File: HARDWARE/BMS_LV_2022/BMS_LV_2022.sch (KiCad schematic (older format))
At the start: 30 parts, among them J1 Conn_01x06_Male, J2 Conn_01x12_Male, J3 USB_B_Mini, J4 Battery+, J5 Battery-, SW1 SW_Push, U1 STM32L4P5RET6, Y1 Crystal

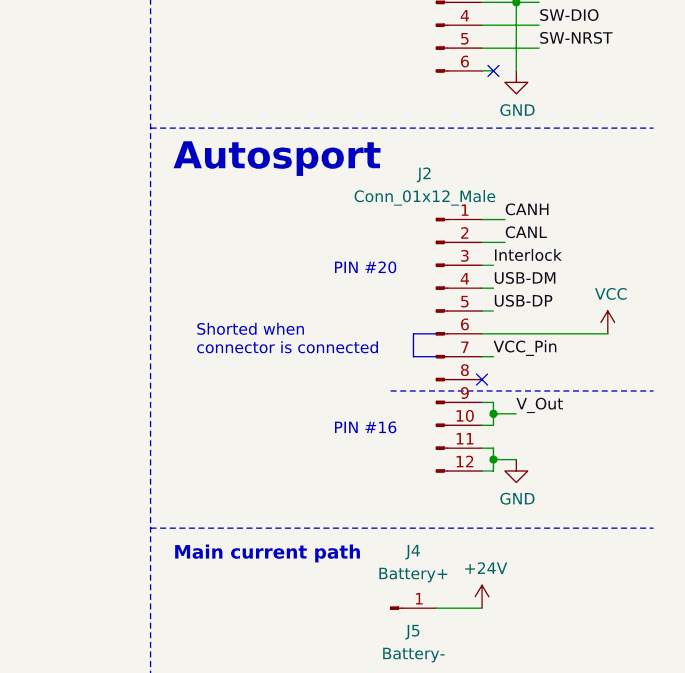
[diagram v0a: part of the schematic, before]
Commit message: PCB Routing Update
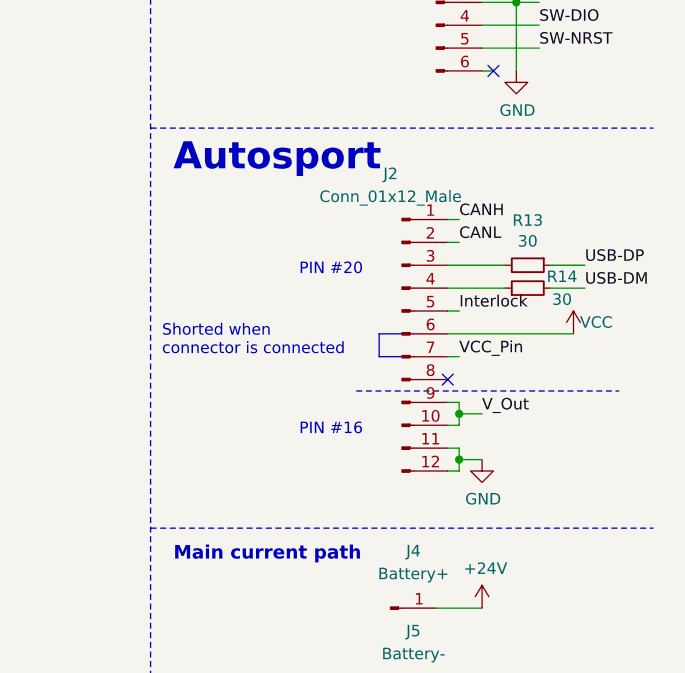
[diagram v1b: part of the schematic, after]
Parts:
- added R13, R14: 30, Resistor_SMD:R_0603_1608Metric, symbol Device:R_Small
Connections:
- net Interlock: now also J2.5 (Pin_5); no longer J2.3 (Pin_3)
- net USB-DM: now also R14.2; no longer J2.4 (Pin_4)
- net USB-DP: now also R13.1; no longer J2.5 (Pin_5)
- new net: J2.3 (Pin_3), R13.2
- new net: J2.4 (Pin_4), R14.1
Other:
- moved on the sheet: J2
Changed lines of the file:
@@
 EESchema Schematic File Version 4
-LIBS:BMS_LV_2022-cache
-EELAYER 29 0
+EELAYER 30 0
 EELAYER END
 $Descr A4 11693 8268
@@
 L Connector:Conn_01x12_Male J2
 U 1 1 61E8A62C
-P 10250 4150
-F 0 "J2" H 10200 4850 50  0000 C CNN
-F 1 "Conn_01x12_Male" H 10200 4750 50  0000 C CNN
-F 2 "footprints:AS214-97PN" H 10250 4150 50  0001 C CNN
-F 3 "~" H 10250 4150 50  0001 C CNN
-	1    10250 4150
+P 10100 4150
+F 0 "J2" H 10050 4850 50  0000 C CNN
+F 1 "Conn_01x12_Male" H 10050 4750 50  0000 C CNN
+F 2 "footprints:AS214-97PN" H 10100 4150 50  0001 C CNN
+F 3 "~" H 10100 4150 50  0001 C CNN
+	1    10100 4150
 	1    0    0    -1
 $EndComp
@@
 Text Label 800  4650 2    50   ~ 0
 CANL
-Text Label 10550 3650 0    50   ~ 0
+Text Label 10350 3650 0    50   ~ 0
 CANH
-Text Label 10550 3750 0    50   ~ 0
+Text Label 10350 3750 0    50   ~ 0
 CANL
-Wire Wire Line
-	10550 3650 10450 3650
-Wire Wire Line
-	10450 3750 10550 3750
 $Sheet
 S 550  2950 1050 500
@@
 Text Label 7000 4300 0    50   ~ 0
 Interlock
-Text Label 10500 3850 0    50   ~ 0
+Text Label 10350 4050 0    50   ~ 0
 Interlock
 Wire Wire Line
-	10450 3850 10500 3850
+	10300 4050 10350 4050
 Wire Wire Line
 	1600 3350 1650 3350
 Text Label 1650 3350 0    50   ~ 0
 CS_IP+
-Text Label 10600 4500 0    50   ~ 0
+Text Label 10450 4500 0    50   ~ 0
 V_Out
 Wire Wire Line
-	10450 4750 10500 4750
+	10300 4750 10350 4750
 $Comp
 L power:GND #PWR010
 U 1 1 62A04D91
-P 10600 4700
-F 0 "#PWR010" H 10600 4450 50  0001 C CNN
-F 1 "GND" H 10605 4527 50  0000 C CNN
-F 2 "" H 10600 4700 50  0001 C CNN
-F 3 "" H 10600 4700 50  0001 C CNN
-	1    10600 4700
-	1    0    0    -1
-$EndComp
-Wire Wire Line
-	10500 4550 10450 4550
-Text Notes 9200 4250 0    50   ~ 0
+P 10450 4700
+F 0 "#PWR010" H 10450 4450 50  0001 C CNN
+F 1 "GND" H 10455 4527 50  0000 C CNN
+F 2 "" H 10450 4700 50  0001 C CNN
+F 3 "" H 10450 4700 50  0001 C CNN
+	1    10450 4700
+	1    0    0    -1
+$EndComp
+Wire Wire Line
+	10350 4550 10300 4550
+Text Notes 9050 4250 0    50   ~ 0
 Shorted when \nconnector is connected
 Text Notes 9450 700  0    157  ~ 31
@@
 VCC_Pin
 Wire Wire Line
-	10450 4250 10500 4250
-Text Label 10500 4250 0    50   ~ 0
+	10300 4250 10350 4250
+Text Label 10350 4250 0    50   ~ 0
 VCC_Pin
 Wire Bus Line
-	10250 4250 10150 4250
+	10100 4250 10000 4250
 Wire Bus Line
-	10150 4250 10150 4150
+	10000 4250 10000 4150
 Wire Bus Line
-	10150 4150 10250 4150
+	10000 4150 10100 4150
 Wire Notes Line
-	10050 4400 11200 4400
-Text Notes 9800 3900 0    50   ~ 0
+	9900 4400 11050 4400
+Text Notes 9650 3900 0    50   ~ 0
 PIN #20
-Text Notes 9800 4600 0    50   ~ 0
+Text Notes 9650 4600 0    50   ~ 0
 PIN #16
-Text Label 10500 3950 0    50   ~ 0
-USB-DM
-Text Label 10500 4050 0    50   ~ 0
-USB-DP
-Wire Wire Line
-	10450 3950 10500 3950
-Wire Wire Line
-	10450 4050 10500 4050
 NoConn ~ 5550 5300
 NoConn ~ 5550 5400
@@
 NoConn ~ 6950 5500
 NoConn ~ 6950 5600
-NoConn ~ 10450 4350
+NoConn ~ 10300 4350
 NoConn ~ 10350 1500
 Text Notes 1200 5200 0    118  ~ 0
@@
 	6150 1800 6150 1700
 Wire Wire Line
-	10450 4150 11000 4150
+	10300 4150 10850 4150
 $Comp
 L power:VCC #PWR014
 U 1 1 622C0542
-P 11000 4150
-F 0 "#PWR014" H 11000 4000 50  0001 C CNN
-F 1 "VCC" H 11015 4323 50  0000 C CNN
-F 2 "" H 11000 4150 50  0001 C CNN
-F 3 "" H 11000 4150 50  0001 C CNN
-	1    11000 4150
-	1    0    0    -1
-$EndComp
-Wire Wire Line
-	10500 4450 10450 4450
-Wire Wire Line
-	10500 4450 10500 4500
-Wire Wire Line
-	10500 4500 10600 4500
-Connection ~ 10500 4500
-Wire Wire Line
-	10500 4500 10500 4550
-Wire Wire Line
-	10500 4750 10500 4700
-Wire Wire Line
-	10500 4650 10450 4650
-Wire Wire Line
-	10500 4700 10600 4700
-Connection ~ 10500 4700
-Wire Wire Line
-	10500 4700 10500 4650
+P 10850 4150
+F 0 "#PWR014" H 10850 4000 50  0001 C CNN
+F 1 "VCC" H 10950 4200 50  0000 C CNN
+F 2 "" H 10850 4150 50  0001 C CNN
+F 3 "" H 10850 4150 50  0001 C CNN
+	1    10850 4150
+	1    0    0    -1
+$EndComp
+Wire Wire Line
+	10350 4450 10300 4450
+Wire Wire Line
+	10350 4450 10350 4500
+Wire Wire Line
+	10350 4500 10450 4500
+Connection ~ 10350 4500
+Wire Wire Line
+	10350 4500 10350 4550
+Wire Wire Line
+	10350 4750 10350 4700
+Wire Wire Line
+	10350 4650 10300 4650
+Wire Wire Line
+	10350 4700 10450 4700
+Connection ~ 10350 4700
+Wire Wire Line
+	10350 4700 10350 4650
 $Comp
 L Device:Crystal_GND24_Small Y1
@@
 	1    0    0    -1
 $EndComp
+$Comp
+L Device:R_Small R14
+U 1 1 61EF25B8
+P 10650 3950
+F 0 "R14" V 10700 3800 50  0000 C CNN
+F 1 "30" V 10600 3800 50  0000 C CNN
+F 2 "Resistor_SMD:R_0603_1608Metric" H 10650 3950 50  0001 C CNN
+F 3 "~" H 10650 3950 50  0001 C CNN
+	1    10650 3950
+	0    -1   -1   0
+$EndComp
+Wire Wire Line
+	10900 3950 10750 3950
+Wire Wire Line
+	10900 3850 10750 3850
+Text Label 10900 3950 0    50   ~ 0
+USB-DM
+Text Label 10900 3850 0    50   ~ 0
+USB-DP
+$Comp
+L Device:R_Small R13
+U 1 1 61EF25C3
+P 10650 3850
+F 0 "R13" V 10454 3850 50  0000 C CNN
+F 1 "30" V 10545 3850 50  0000 C CNN
+F 2 "Resistor_SMD:R_0603_1608Metric" H 10650 3850 50  0001 C CNN
+F 3 "~" H 10650 3850 50  0001 C CNN
+	1    10650 3850
+	0    1    1    0
+$EndComp
+Wire Wire Line
+	10300 3650 10350 3650
+Wire Wire Line
+	10300 3750 10350 3750
+Wire Wire Line
+	10550 3950 10300 3950
+Wire Wire Line
+	10550 3850 10300 3850
 $EndSCHEMATC

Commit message: PCB Routing Update 2
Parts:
- U1: symbol BMS_LV_2022-rescue:STM32L4P5RET6-STM32L4P5RET6 -> stm32l4p5ret6:STM32L4P5RET6-STM32L4P5RET6
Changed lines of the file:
@@
 CS
 $Comp
-L BMS_LV_2022-rescue:STM32L4P5RET6-STM32L4P5RET6 U1
+L stm32l4p5ret6:STM32L4P5RET6-STM32L4P5RET6 U1
 U 1 1 61992FF1
 P 6250 3900

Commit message: Small bug fixes
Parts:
- U1: symbol stm32l4p5ret6:STM32L4P5RET6-STM32L4P5RET6 -> BMS_LV_2022-rescue:STM32L4P5RET6-STM32L4P5RET6-stm32l4p5ret6
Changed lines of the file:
@@
 CS
 $Comp
-L stm32l4p5ret6:STM32L4P5RET6-STM32L4P5RET6 U1
+L BMS_LV_2022-rescue:STM32L4P5RET6-STM32L4P5RET6-stm32l4p5ret6 U1
 U 1 1 61992FF1
 P 6250 3900

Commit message: HARDWARE Release V1.0
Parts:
- added R15: 1k, Resistor_SMD:R_0603_1608Metric, symbol Device:R_Small
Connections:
- net Interlock: now also R15.2; no longer J2.5 (Pin_5)
- net Therm_1: now also U1.17 (PA3); no longer U1.20 (PA4)
- net Therm_2: now also U1.20 (PA4); no longer U1.21 (PA5)
- net Therm_3: now also U1.21 (PA5); no longer U1.22 (PA6)
- net Therm_4: now also U1.22 (PA6); no longer U1.23 (PA7)
- net Therm_5: now also U1.23 (PA7); no longer U1.24 (PC4)
- net Therm_6: now also U1.24 (PC4); no longer U1.25 (PC5)
- net Therm_8: now reaches U1.26 (PB0)
- new net: J2.5 (Pin_5), R15.1
- new net Therm_7: U1.25 (PC5)
- no-connect marks 29 -> 27
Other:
- moved on the sheet: C1, D1, D3, D4, D5, R1, R2, R3, R5, R6, SW1

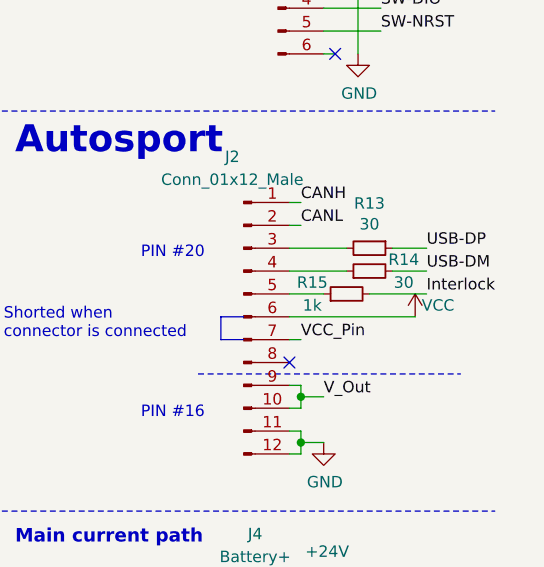
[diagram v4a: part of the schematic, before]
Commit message: Changes in V1.0
-Fuse holder change
-Autosport conn angle change
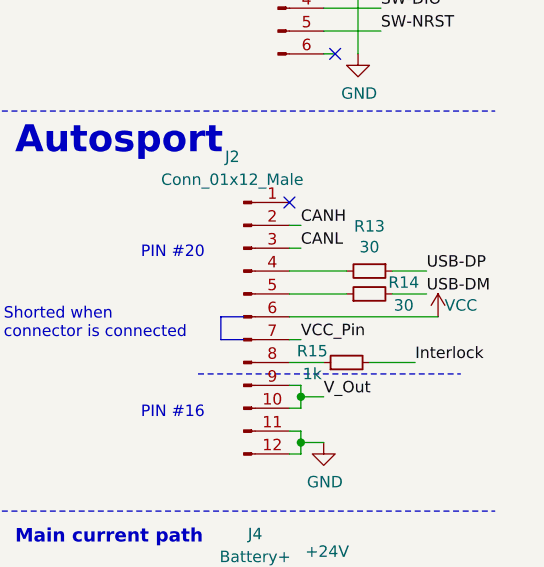
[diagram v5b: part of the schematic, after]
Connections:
- net CANH: now also J2.2 (Pin_2); no longer J2.1 (Pin_1)
- net CANL: now also J2.3 (Pin_3); no longer J2.2 (Pin_2)
- net at R13.2: now also J2.4 (Pin_4); no longer J2.3 (Pin_3)
- net at R14.1: now also J2.5 (Pin_5); no longer J2.4 (Pin_4)
- net at R15.1: now also J2.8 (Pin_8); no longer J2.5 (Pin_5)
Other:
- moved on the sheet: R13, R14, R15
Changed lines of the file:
@@
 Text Label 800  4800 2    50   ~ 0
 CANL
-Text Label 10350 3650 0    50   ~ 0
+Text Label 10350 3750 0    50   ~ 0
 CANH
-Text Label 10350 3750 0    50   ~ 0
+Text Label 10350 3850 0    50   ~ 0
 CANL
 $Sheet
@@
 Text Label 7000 4300 0    50   ~ 0
 Interlock
-Text Label 10900 4050 0    50   ~ 0
+Text Label 10850 4350 0    50   ~ 0
 Interlock
 Wire Wire Line
@@
 NoConn ~ 6950 5500
 NoConn ~ 6950 5600
-NoConn ~ 10300 4350
+NoConn ~ 10300 3650
 NoConn ~ 10350 1500
 Text Notes 1200 5350 0    118  ~ 0
@@
 Wire Wire Line
 	6150 1800 6150 1700
-Wire Wire Line
-	10300 4150 10850 4150
 $Comp
 L power:VCC #PWR014
 U 1 1 622C0542
-P 10850 4150
-F 0 "#PWR014" H 10850 4000 50  0001 C CNN
-F 1 "VCC" H 10950 4200 50  0000 C CNN
-F 2 "" H 10850 4150 50  0001 C CNN
-F 3 "" H 10850 4150 50  0001 C CNN
-	1    10850 4150
+P 10950 4150
+F 0 "#PWR014" H 10950 4000 50  0001 C CNN
+F 1 "VCC" H 11050 4200 50  0000 C CNN
+F 2 "" H 10950 4150 50  0001 C CNN
+F 3 "" H 10950 4150 50  0001 C CNN
+	1    10950 4150
 	1    0    0    -1
 $EndComp
@@
 L Device:R_Small R14
 U 1 1 61EF25B8
+P 10650 4050
+F 0 "R14" V 10700 3900 50  0000 C CNN
+F 1 "30" V 10600 3900 50  0000 C CNN
+F 2 "Resistor_SMD:R_0603_1608Metric" H 10650 4050 50  0001 C CNN
+F 3 "~" H 10650 4050 50  0001 C CNN
+	1    10650 4050
+	0    -1   -1   0
+$EndComp
+Wire Wire Line
+	10900 4050 10750 4050
+Wire Wire Line
+	10900 3950 10750 3950
+Text Label 10900 4050 0    50   ~ 0
+USB-DM
+Text Label 10900 3950 0    50   ~ 0
+USB-DP
+$Comp
+L Device:R_Small R13
+U 1 1 61EF25C3
 P 10650 3950
-F 0 "R14" V 10700 3800 50  0000 C CNN
-F 1 "30" V 10600 3800 50  0000 C CNN
+F 0 "R13" V 10454 3950 50  0000 C CNN
+F 1 "30" V 10545 3950 50  0000 C CNN
 F 2 "Resistor_SMD:R_0603_1608Metric" H 10650 3950 50  0001 C CNN
 F 3 "~" H 10650 3950 50  0001 C CNN
 	1    10650 3950
-	0    -1   -1   0
-$EndComp
-Wire Wire Line
-	10900 3950 10750 3950
-Wire Wire Line
-	10900 3850 10750 3850
-Text Label 10900 3950 0    50   ~ 0
-USB-DM
-Text Label 10900 3850 0    50   ~ 0
-USB-DP
-$Comp
-L Device:R_Small R13
-U 1 1 61EF25C3
-P 10650 3850
-F 0 "R13" V 10454 3850 50  0000 C CNN
-F 1 "30" V 10545 3850 50  0000 C CNN
-F 2 "Resistor_SMD:R_0603_1608Metric" H 10650 3850 50  0001 C CNN
-F 3 "~" H 10650 3850 50  0001 C CNN
-	1    10650 3850
 	0    1    1    0
 $EndComp
 Wire Wire Line
-	10300 3650 10350 3650
-Wire Wire Line
 	10300 3750 10350 3750
 Wire Wire Line
+	10300 3850 10350 3850
+Wire Wire Line
+	10550 4050 10300 4050
+Wire Wire Line
 	10550 3950 10300 3950
-Wire Wire Line
-	10550 3850 10300 3850
 $Comp
 L Device:R_Small R15
 U 1 1 61EFA5E6
-P 10550 4050
-F 0 "R15" V 10600 4200 50  0000 C CNN
-F 1 "1k" V 10500 4200 50  0000 C CNN
-F 2 "Resistor_SMD:R_0603_1608Metric" H 10550 4050 50  0001 C CNN
-F 3 "~" H 10550 4050 50  0001 C CNN
-	1    10550 4050
+P 10550 4350
+F 0 "R15" V 10600 4500 50  0000 C CNN
+F 1 "1k" V 10500 4500 50  0000 C CNN
+F 2 "Resistor_SMD:R_0603_1608Metric" H 10550 4350 50  0001 C CNN
+F 3 "~" H 10550 4350 50  0001 C CNN
+	1    10550 4350
 	0    -1   -1   0
 $EndComp
 Wire Wire Line
-	10300 4050 10450 4050
-Wire Wire Line
-	10650 4050 10900 4050
+	10300 4350 10450 4350
 Wire Notes Line
 	2300 5100 2300 7800
@@
 Text Label 7000 4100 0    50   ~ 0
 Therm_8
+Wire Wire Line
+	10850 4350 10650 4350
+Wire Wire Line
+	10300 4150 10950 4150
 $EndSCHEMATC

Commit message: Last Changes in V1.0
Fuse voltage measurement added
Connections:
- net VoltageFuseMeasure: now reaches U1.30 (PB11)
- no-connect marks 27 -> 26
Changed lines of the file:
@@
 $EndDescr
 $Sheet
-S 550  1350 700  450
+S 550  1300 700  450
 U 61996AA1
 F0 "LTC6810" 50
 F1 "LTC6810.sch" 50
-F2 "MOSI" I R 1250 1400 50
-F3 "MISO" O R 1250 1500 50
-F4 "SCK" I R 1250 1600 50
-F5 "CS" I R 1250 1700 50
+F2 "MOSI" I R 1250 1350 50
+F3 "MISO" O R 1250 1450 50
+F4 "SCK" I R 1250 1550 50
+F5 "CS" I R 1250 1650 50
 $EndSheet
 $Comp
@@
 	6250 5850 6250 5900
 $Sheet
-S 550  2050 800  850
+S 550  1950 800  850
 U 61D09503
 F0 "Thermistors" 50
 F1 "Thermistors.sch" 50
-F2 "Therm_1" O R 1350 2100 50
-F3 "Therm_2" O R 1350 2200 50
-F4 "Therm_3" O R 1350 2300 50
-F5 "Therm_4" O R 1350 2400 50
-F6 "Therm_5" O R 1350 2500 50
-F7 "Therm_6" O R 1350 2600 50
-F8 "Therm_7" O R 1350 2700 50
-F9 "Therm_8" O R 1350 2800 50
+F2 "Therm_1" O R 1350 2000 50
+F3 "Therm_2" O R 1350 2100 50
+F4 "Therm_3" O R 1350 2200 50
+F5 "Therm_4" O R 1350 2300 50
+F6 "Therm_5" O R 1350 2400 50
+F7 "Therm_6" O R 1350 2500 50
+F8 "Therm_7" O R 1350 2600 50
+F9 "Therm_8" O R 1350 2700 50
 $EndSheet
-$Sheet
-S 850  4500 900  450
-U 61F4D531
-F0 "CAN" 50
-F1 "CAN.sch" 50
-F2 "CAN-RX" O R 1750 4600 50
-F3 "CAN-TX" I R 1750 4800 50
-F4 "CANH" B L 850 4600 50
-F5 "CANL" B L 850 4800 50
-$EndSheet
-Text Label 1300 1400 0    50   ~ 0
+Text Label 1300 1350 0    50   ~ 0
 MOSI
 Wire Wire Line
-	1250 1400 1300 1400
+	1250 1350 1300 1350
 Wire Wire Line
 	6950 4600 7000 4600
@@
 MOSI
 Wire Wire Line
-	1250 1500 1300 1500
-Wire Wire Line
-	1250 1600 1300 1600
-Wire Wire Line
-	1250 1700 1300 1700
+	1250 1450 1300 1450
+Wire Wire Line
+	1250 1550 1300 1550
+Wire Wire Line
+	1250 1650 1300 1650
+Wire Wire Line
+	1350 2000 1400 2000
 Wire Wire Line
 	1350 2100 1400 2100
@@
 Wire Wire Line
 	1350 2500 1400 2500
-Wire Wire Line
-	1350 2600 1400 2600
-Text Label 1300 1500 0    50   ~ 0
+Text Label 1300 1450 0    50   ~ 0
 MISO
-Text Label 1300 1600 0    50   ~ 0
+Text Label 1300 1550 0    50   ~ 0
 SCK
-Text Label 1300 1700 0    50   ~ 0
+Text Label 1300 1650 0    50   ~ 0
 CS
+Text Label 1400 2000 0    50   ~ 0
+Therm_1
 Text Label 1400 2100 0    50   ~ 0
-Therm_1
+Therm_2
 Text Label 1400 2200 0    50   ~ 0
-Therm_2
+Therm_3
 Text Label 1400 2300 0    50   ~ 0
-Therm_3
+Therm_4
 Text Label 1400 2400 0    50   ~ 0
-Therm_4
+Therm_5
 Text Label 1400 2500 0    50   ~ 0
-Therm_5
-Text Label 1400 2600 0    50   ~ 0
 Therm_6
 Wire Wire Line
@@
 Wire Wire Line
 	6950 5000 7000 5000
-Text Label 1800 4600 0    50   ~ 0
-CAN-RX
-Text Label 1800 4800 0    50   ~ 0
-CAN-TX
-Wire Wire Line
-	1750 4600 1800 4600
-Wire Wire Line
-	1750 4800 1800 4800
 Text Label 7000 4900 0    50   ~ 0
 CAN-RX
@@
 	1    0    0    -1
 $EndComp
-Wire Wire Line
-	850  4600 800  4600
-Wire Wire Line
-	850  4800 800  4800
-Text Label 800  4600 2    50   ~ 0
-CANH
-Text Label 800  4800 2    50   ~ 0
-CANL
 Text Label 10350 3750 0    50   ~ 0
 CANH
 Text Label 10350 3850 0    50   ~ 0
 CANL
-$Sheet
-S 550  3150 1050 500
-U 6269845F
-F0 "eFuse" 50
-F1 "eFuse.sch" 50
-F2 "Switch_Signal" I R 1600 3250 50
-F3 "CurrentSensor_IP+" O R 1600 3550 50
-F4 "VCC_Pin" I R 1600 3400 50
-$EndSheet
-Wire Wire Line
-	1600 3250 1650 3250
-Text Label 1650 3250 0    50   ~ 0
+Wire Wire Line
+	1600 3100 1650 3100
+Text Label 1650 3100 0    50   ~ 0
 Switch_Signal
 Text Label 7000 2600 0    50   ~ 0
@@
 Interlock
 Wire Wire Line
-	1600 3550 1650 3550
-Text Label 1650 3550 0    50   ~ 0
+	1600 3400 1650 3400
+Text Label 1650 3400 0    50   ~ 0
 CS_IP+
 Text Label 10450 4500 0    50   ~ 0
@@
 Wire Wire Line
 	850  5500 850  5450
-Text Label 1950 4150 0    50   ~ 0
-CurrentSensor_Out
-Text Label 1950 4000 0    50   ~ 0
+Text Label 1950 4050 0    50   ~ 0
 V_Out
 Wire Wire Line
-	1900 4150 1950 4150
-Wire Wire Line
-	1900 4000 1950 4000
-Text Label 800  4050 2    50   ~ 0
-CS_IP+
-Wire Wire Line
-	850  4050 800  4050
-$Sheet
-S 850  3850 1050 450
-U 62C2DD72
-F0 "CurrentSensor" 50
-F1 "CurrentSensor.sch" 50
-F2 "CS_IP+" I L 850 4050 50
-F3 "V_Out" O R 1900 4000 50
-F4 "CurrentSensor" O R 1900 4150 50
-$EndSheet
+	1900 4050 1950 4050
 Wire Wire Line
 	1700 5300 1700 5500
@@
 	2300 6200 500  6200
 Wire Wire Line
-	1600 3400 1650 3400
-Text Label 1650 3400 0    50   ~ 0
+	1600 3250 1650 3250
+Text Label 1650 3250 0    50   ~ 0
 VCC_Pin
 Wire Wire Line
@@
 NoConn ~ 6950 4800
 NoConn ~ 6950 5100
-NoConn ~ 6950 5200
 NoConn ~ 6950 5300
 NoConn ~ 6950 5400
@@
 	2300 5100 2300 7800
 Wire Wire Line
+	1350 2600 1400 2600
+Wire Wire Line
 	1350 2700 1400 2700
-Wire Wire Line
-	1350 2800 1400 2800
+Text Label 1400 2600 0    50   ~ 0
+Therm_7
 Text Label 1400 2700 0    50   ~ 0
-Therm_7
-Text Label 1400 2800 0    50   ~ 0
 Therm_8
 Text Label 7000 3100 0    50   ~ 0
@@
 Wire Wire Line
 	10300 4150 10950 4150
+$Sheet
+S 850  3900 1050 450
+U 62C2DD72
+F0 "CurrentSensor" 50
+F1 "CurrentSensor.sch" 50
+F2 "CS_IP+" I L 850 4100 50
+F3 "V_Out" O R 1900 4050 50
+F4 "CurrentSensor" O R 1900 4200 50
+$EndSheet
+Wire Wire Line
+	850  4100 800  4100
+Text Label 800  4100 2    50   ~ 0
+CS_IP+
+Wire Wire Line
+	1900 4200 1950 4200
+Text Label 1950 4200 0    50   ~ 0
+CurrentSensor_Out
+Text Label 800  4850 2    50   ~ 0
+CANL
+Text Label 800  4650 2    50   ~ 0
+CANH
+Wire Wire Line
+	850  4850 800  4850
+Wire Wire Line
+	850  4650 800  4650
+Wire Wire Line
+	1750 4850 1800 4850
+Wire Wire Line
+	1750 4650 1800 4650
+Text Label 1800 4850 0    50   ~ 0
+CAN-TX
+Text Label 1800 4650 0    50   ~ 0
+CAN-RX
+$Sheet
+S 850  4550 900  450
+U 61F4D531
+F0 "CAN" 50
+F1 "CAN.sch" 50
+F2 "CAN-RX" O R 1750 4650 50
+F3 "CAN-TX" I R 1750 4850 50
+F4 "CANH" B L 850 4650 50
+F5 "CANL" B L 850 4850 50
+$EndSheet
+$Sheet
+S 550  3000 1050 650
+U 6269845F
+F0 "eFuse" 50
+F1 "eFuse.sch" 50
+F2 "Switch_Signal" I R 1600 3100 50
+F3 "CurrentSensor_IP+" O R 1600 3400 50
+F4 "VCC_Pin" I R 1600 3250 50
+F5 "VoltageFuseMeasure" O R 1600 3550 50
+$EndSheet
+Wire Wire Line
+	1600 3550 1650 3550
+Text Label 1650 3550 0    50   ~ 0
+VoltageFuseMeasure
+Wire Wire Line
+	6950 5200 7000 5200
+Text Label 7000 5200 0    50   ~ 0
+VoltageFuseMeasure
 $EndSCHEMATC
